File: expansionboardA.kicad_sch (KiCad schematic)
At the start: 40 parts, among them J1 USB-SERIAL, J3 HDMI_A, P1 USB_C_Plug, U1 MAX3420EECJ, U2 GPIO_U2, U3 AMS1117-3.3, U4 GPIO_U4, U5 MCP3008T-I/SL, U6 TLV320AIC23BIPW, Y1 Crystal

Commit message: Board updated
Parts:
- J1: value USB-SERIAL -> DEBUG
- renumbered MicroSDCard1 to CRD1
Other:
- note removed: "An expansion board for QMTECH A7200T core board"
- note removed: "QMTECH A7200T Board Expansion Module"
- note removed: "v0.1"
- moved on the sheet: ADC1, AU1, AU2, C1, C2, C3, C4, C5, C6, C7, D1, D2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

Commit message: Updated schematic with correct parts Built gerber files
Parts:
- C6, C7: footprint Capacitor_SMD:C_0603_1608Metric -> Capacitor_SMD:C_0805_2012Metric_Pad1.18x1.45mm_HandSolder
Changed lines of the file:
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@@
       (effects (font (size 1.27 1.27)) (justify left))
     )
-    (property "Footprint" "Capacitor_SMD:C_0603_1608Metric" (at 274.0152 49.53 0)
+    (property "Footprint" "Capacitor_SMD:C_0805_2012Metric_Pad1.18x1.45mm_HandSolder" (at 274.0152 49.53 0)
       (effects (font (size 1.27 1.27)) hide)
     )
@@
       (effects (font (size 1.27 1.27)) (justify left))
     )
-    (property "Footprint" "Capacitor_SMD:C_0603_1608Metric" (at 294.3352 49.53 0)
-      (effects (font (size 1.27 1.27)) hide)
-    )
+    (property "Footprint" "Capacitor_SMD:C_0805_2012Metric_Pad1.18x1.45mm_HandSolder" (at 294.3352 49.53 0)
+      (effects (font (size 1.27 1.27)) hide)
+    )

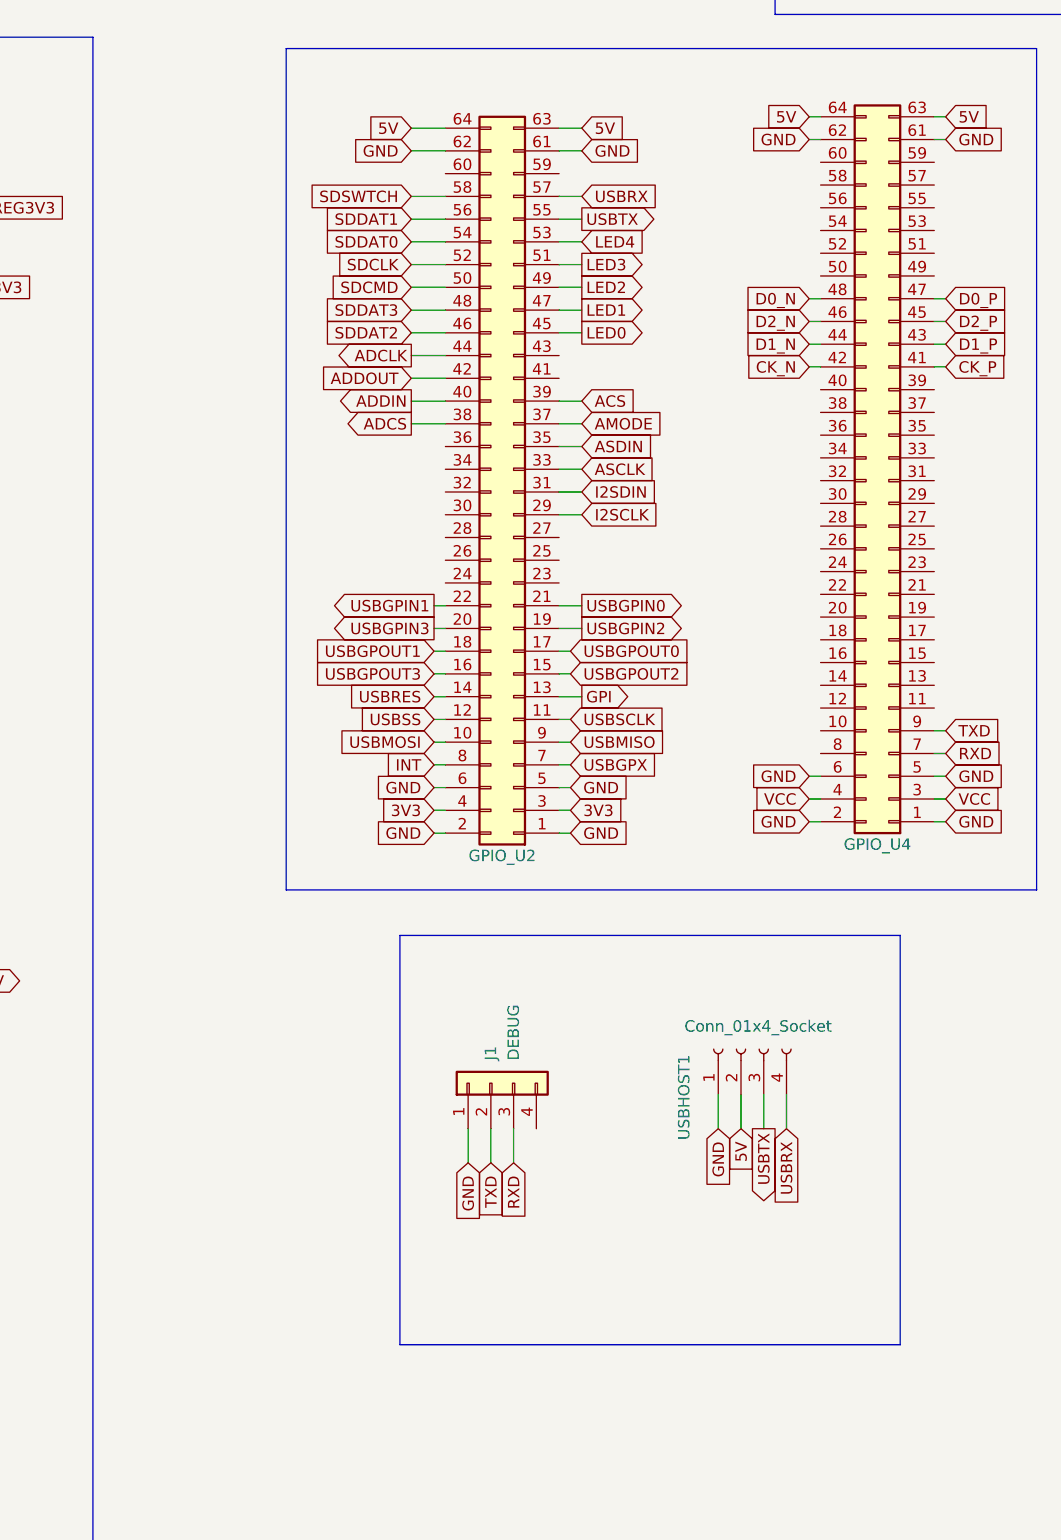
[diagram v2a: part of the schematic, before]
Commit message: Updated board with USB A host connector
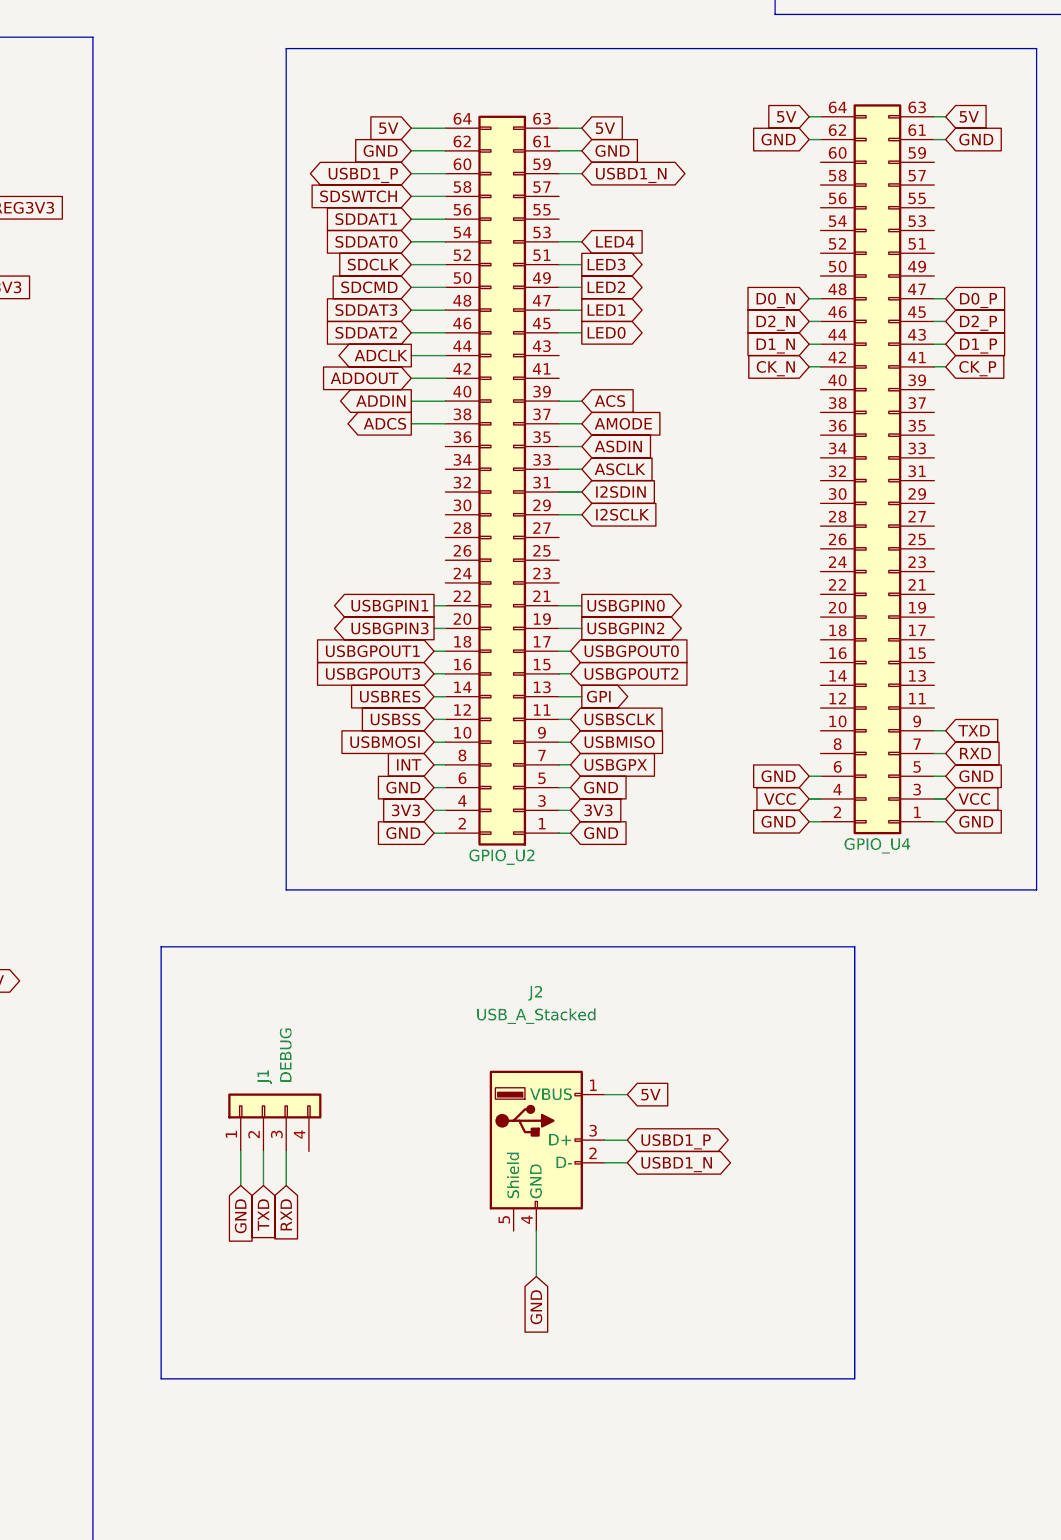
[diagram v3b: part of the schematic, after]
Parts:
- removed USBHOST1: Conn_01x4_Socket, Connector_PinSocket_2.54mm:PinSocket_1x04_P2.54mm_Horizontal, symbol Connector:Conn_01x04_Socket
- added J2: USB_A_Stacked, Connector_USB:USB_A_Molex_67643_Horizontal, symbol Connector:USB_A
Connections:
- net 5V: now also J2.1 (VBUS)
- net GND: now also J2.4 (GND)
- net USBD1_N: now reaches U2.59 (Pin_59)
- net USBD1_N: now also J2.2 (D-)
- net USBD1_P: now reaches U2.60 (Pin_60)
- net USBD1_P: now also J2.3 (D+)
- net USBRX: no longer names the net of U2.57 (Pin_57)
- net USBTX: no longer names the net of U2.55 (Pin_55)
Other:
- moved on the sheet: J1

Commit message: Updated board
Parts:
- C1, C2, C3, C4, C5: footprint Capacitor_SMD:C_0603_1608Metric -> Capacitor_SMD:C_0603_1608Metric_Pad1.08x0.95mm_HandSolder
- R1, R10, R2, R3, R4, R5, R6, R7, R9: footprint Resistor_SMD:R_0603_1608Metric -> Resistor_SMD:R_0603_1608Metric_Pad0.98x0.95mm_HandSolder
- U3: footprint Package_TO_SOT_SMD:SOT-89-3 -> Package_TO_SOT_SMD:SOT-89-3_Handsoldering

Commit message: Updatre board version
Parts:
- removed AU2: SJ-3523-SMT-TR, SJ-3523-SMT-TR:CUI_SJ-3523-SMT-TR, symbol SJ-3523-SMT-TR:SJ-3523-SMT-TR
- removed D6: LED, LED_SMD:LED_1206_3216Metric_Pad1.42x1.75mm_HandSolder, symbol Device:LED
- removed U6: TLV320AIC23BIPW, TLV320AIC23BIPW:SOP65P640X120-28N, symbol TLV320AIC23BIPW:TLV320AIC23BIPW
- added C10: 0.1uf, Capacitor_SMD:C_0603_1608Metric_Pad1.08x0.95mm_HandSolder, symbol Device:C
- added C11, C13, C14: 3.3uf, Capacitor_THT:CP_Radial_D5.0mm_P2.50mm, symbol Device:C_Polarized_US
- added C12: 10uf, Capacitor_THT:CP_Radial_D5.0mm_P2.50mm, symbol Device:C_Polarized_US
- added C8, C9: 1uf ceramic, Capacitor_SMD:C_0603_1608Metric_Pad1.08x0.95mm_HandSolder, symbol Device:C
- added R11, R14: 10KOhm, Resistor_SMD:R_0603_1608Metric_Pad0.98x0.95mm_HandSolder, symbol Device:R
- added R12, R13: 470Ohm, Resistor_SMD:R_0603_1608Metric_Pad0.98x0.95mm_HandSolder, symbol Device:R
- added R8: R33_ohm, Resistor_SMD:R_0603_1608Metric_Pad0.98x0.95mm_HandSolder, symbol Device:R
- added U6: CS4344-CZZR, CIR_3TSSOP-10, symbol 2023-04-16_23-08-01:CS4344-CZZR
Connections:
- net HPOUTLEFT is gone; now on an unnamed net: AU1.3
- net GND: now also C10.2, C11.2, C12.2, C8.1, C9.2, R11.2, R14.2, U6.8 (GND)
- net at R7.2: now also C8.2
- net ACS: no longer names the net of U2.39 (Pin_39)
- net AMODE: no longer names the net of U2.37 (Pin_37)
- net ASCLK renamed AU_LRCLK
- net AU_LRCLK: now also U6.3 (LRCK)
- net ASDIN renamed AU_MCLK
- net AU_MCLK: now also U6.4 (MCLK)
- net HPOUTRIGHT: no longer names the net of AU1.2
- net HPOUTRIGHT: now also C9.1, R8.2
- net I2SCLK renamed AU_SDIN
- net AU_SDIN: now also U6.1 (SDIN)
- net I2SDIN renamed AU_SCLK
- net AU_SCLK: now also U6.2 (*DEM/SCLK)
- net LED4: no longer names the net of U2.53 (Pin_53)
- net LED4: no longer R7.1
- new net: C13.2, R11.1, R12.1
- new net: C14.2, R13.1, R14.1
- new net: C12.1, U6.6 (FILT+)
- new net: C10.1, C11.1, U6.5 (VQ)
- new net AL: C14.1, U6.7 (AOUTL)
- new net AR: C13.1, U6.10 (AOUTR)
- new net LEFTOUT: R13.2, R7.1
- new net RIGHTOUT: R12.2, R8.1
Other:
- note added: "3v3 Power Regulator"
- note added: "Analog / Digital converter"
- note added: "Audio Out"
- note added: "Audio Output"
- note added: "DVI out over HDMI"
- note added: "Debug LEDs"
- note added: "FPGA board GPIO pins"
- note added: "Micro SD Card"
- note added: "Serial Debug Port"
- note added: "USB-A Host socket"
- note added: "USB-C Power and Data"
- moved on the sheet: ADC1, AU1, C1, C2, C3, C4, C5, C6, C7, CRD1, D1, D2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

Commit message: Updated board to fix some issues
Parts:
- added J4: FAN, Connector_PinHeader_2.54mm:PinHeader_1x02_P2.54mm_Vertical, symbol Connector_Generic:Conn_01x02
- J1: footprint Connector_PinSocket_2.54mm:PinSocket_1x04_P2.54mm_Vertical -> Connector_PinSocket_2.54mm:PinSocket_1x04_P2.54mm_Horizontal
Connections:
- net 5V: now also J4.2 (Pin_2)
- net GND: now also J4.1 (Pin_1)
- net input3v3: now also U6.9 (VA)
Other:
- note added: "FPGA Fan"
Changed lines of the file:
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@@
+    (stroke (width 0) (type default))
+  )
+  (wire (pts (xy 172.72 125.73) (xy 172.72 128.27))
     (stroke (width 0) (type default))
   )
@@
     (stroke (width 0) (type default))
   )
+  (wire (pts (xy 379.73 27.94) (xy 383.54 27.94))
+    (stroke (width 0) (type default))
+  )
   (wire (pts (xy 102.87 114.3) (xy 105.41 114.3))
     (stroke (width 0) (type default))
@@
     (stroke (width 0) (type default))
   )
+  (wire (pts (xy 170.18 125.73) (xy 170.18 128.27))
+    (stroke (width 0) (type default))
+  )
   (wire (pts (xy 226.06 53.34) (xy 241.3 53.34))
     (stroke (width 0) (type default))
@@
   )
   (rectangle (start 214.63 15.24) (end 280.67 60.96)
+    (stroke (width 0) (type default))
+    (fill (type none))
+  )
+  (rectangle (start 160.02 111.76) (end 182.88 137.16)
     (stroke (width 0) (type default))
     (fill (type none))
@@
     (effects (font (size 1.27 1.27)) (justify left bottom))
   )
+  (text "FPGA Fan" (at 161.29 114.3 0)
+    (effects (font (size 1.27 1.27)) (justify left bottom))
+  )
   (text "Analog / Digital converter" (at 82.55 17.78 0)
     (effects (font (size 1.27 1.27)) (justify left bottom))
@@
     (effects (font (size 1.27 1.27)) (justify left bottom))
   )
-  (label "input3v3" (at 377.19 27.94 0) (fields_autoplaced)
+  (label "input3v3" (at 383.54 27.94 0) (fields_autoplaced)
     (effects (font (size 1.27 1.27)) (justify left bottom))
   )
@@
     )
   )
+  (global_label "GND" (shape input) (at 170.18 128.27 270) (fields_autoplaced)
+    (effects (font (size 1.27 1.27)) (justify right))
+    (property "Intersheetrefs" "${INTERSHEET_REFS}" (at 170.18 135.0463 90)
+      (effects (font (size 1.27 1.27)) (justify right) hide)
+    )
+  )
   (global_label "GPI" (shape input) (at 308.61 101.6 180) (fields_autoplaced)
     (effects (font (size 1.27 1.27)) (justify right))
@@
     (property "Intersheetrefs" "${INTERSHEET_REFS}" (at 396.6663 45.72 0)
       (effects (font (size 1.27 1.27)) (justify left) hide)
+    )
+  )
+  (global_label "5V" (shape input) (at 172.72 128.27 270) (fields_autoplaced)
+    (effects (font (size 1.27 1.27)) (justify right))
+    (property "Intersheetrefs" "${INTERSHEET_REFS}" (at 172.72 133.4739 90)
+      (effects (font (size 1.27 1.27)) (justify right) hide)
     )
   )
@@
       (effects (font (size 1.27 1.27)) (justify left))
     )
-    (property "Footprint" "Connector_PinSocket_2.54mm:PinSocket_1x04_P2.54mm_Vertical" (at 171.45 82.55 0)
+    (property "Footprint" "Connector_PinSocket_2.54mm:PinSocket_1x04_P2.54mm_Horizontal" (at 171.45 82.55 0)
       (effects (font (size 1.27 1.27)) hide)
     )
@@
         )
       )
+    )
+  )
+  (symbol (lib_id "Connector_Generic:Conn_01x02") (at 170.18 120.65 90) (unit 1)
+    (in_bom yes) (on_board yes) (dnp no)
+    (property "Reference" "J4" (at 170.1799 118.11 0)
+      (effects (font (size 1.27 1.27)) (justify left))
+    )
+    (property "Value" "FAN" (at 172.7199 118.11 0)
+      (effects (font (size 1.27 1.27)) (justify left))
+    )
+    (property "Footprint" "Connector_PinHeader_2.54mm:PinHeader_1x02_P2.54mm_Vertical" (at 170.18 120.65 0)
+      (effects (font (size 1.27 1.27)) hide)
+    )
+    (property "Datasheet" "~" (at 170.18 120.65 0)
+      (effects (font (size 1.27 1.27)) hide)
+    )
+    (pin "1")
+    (pin "2")
+    (instances
+      (project "expansionboardA"
+        (path "/317f7f3e-4535-46d0-9a87-af1bea12706a"
+          (reference "J4") (unit 1)
+        )
+      )

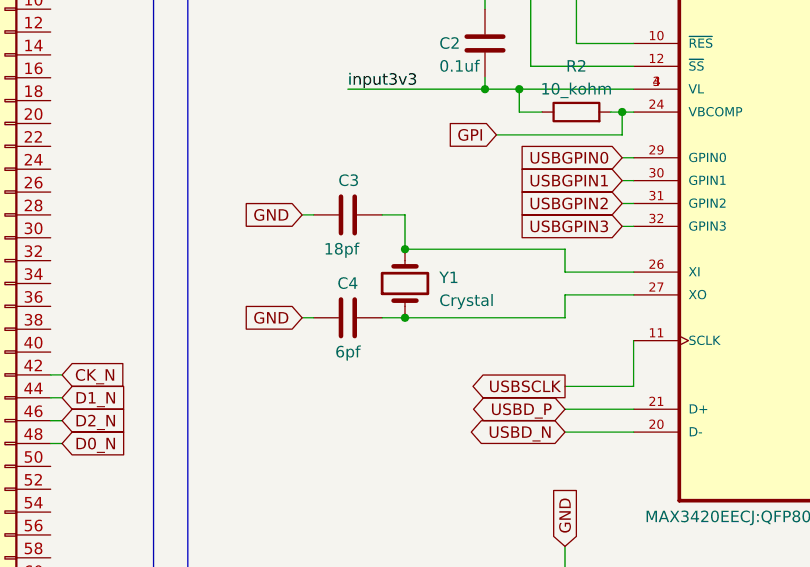
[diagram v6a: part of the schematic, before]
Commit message: Updated to new board version
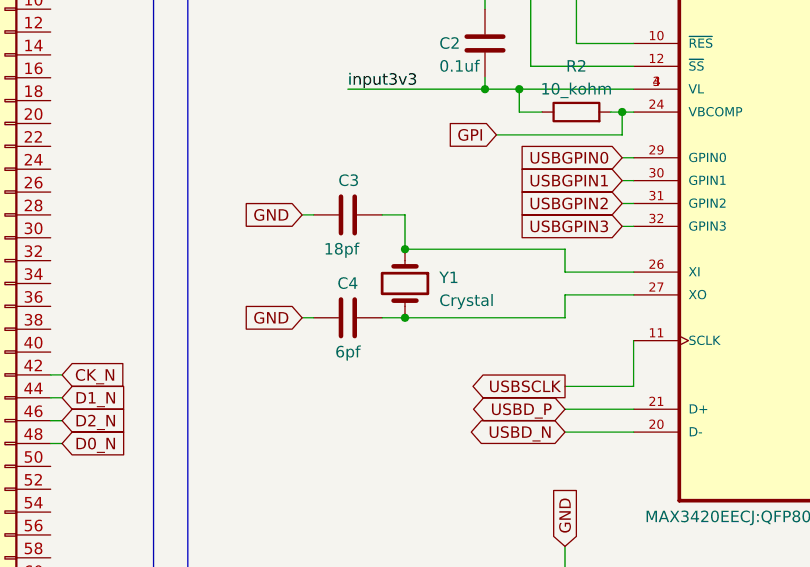
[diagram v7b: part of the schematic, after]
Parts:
- C11, C13, C14: footprint Capacitor_THT:CP_Radial_D5.0mm_P2.50mm -> Capacitor_THT:CP_Radial_D10.0mm_P5.00mm
- C12: footprint Capacitor_THT:CP_Radial_D5.0mm_P2.50mm -> Capacitor_SMD:CP_Elec_6.3x5.9
- R11, R14: footprint Resistor_SMD:R_0603_1608Metric_Pad0.98x0.95mm_HandSolder -> Resistor_THT:R_Axial_DIN0207_L6.3mm_D2.5mm_P7.62mm_Horizontal
- R12, R13: footprint Resistor_SMD:R_0603_1608Metric_Pad0.98x0.95mm_HandSolder -> Resistor_THT:R_Axial_DIN0204_L3.6mm_D1.6mm_P5.08mm_Horizontal
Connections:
- net at C4.2, U1.27 (XO): now also Y1.2; no longer Y1.1
- net at C3.2, U1.26 (XI): now also Y1.1; no longer Y1.2
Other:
- moved on the sheet: Y1
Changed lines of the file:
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@@
   (junction (at 100.33 57.15) (diameter 0) (color 0 0 0 0)
   )
+  (junction (at 298.45 121.92) (diameter 0) (color 0 0 0 0)
+  )
   (junction (at 359.41 57.15) (diameter 0) (color 0 0 0 0)
   )
@@
   (junction (at 323.85 57.15) (diameter 0) (color 0 0 0 0)
   )
-  (junction (at 298.45 121.92) (diameter 0) (color 0 0 0 0)
-  )
   (junction (at 264.16 27.94) (diameter 0) (color 0 0 0 0)
   )
-  (junction (at 119.38 119.38) (diameter 0) (color 0 0 0 0)
-  )
   (junction (at 298.45 114.3) (diameter 0) (color 0 0 0 0)
   )
+  (junction (at 119.38 119.38) (diameter 0) (color 0 0 0 0)
+  )
   (junction (at 307.34 96.52) (diameter 0) (color 0 0 0 0)
   )
@@
     (stroke (width 0) (type default))
   )
-  (wire (pts (xy 298.45 121.92) (xy 316.23 121.92))
+  (wire (pts (xy 295.91 121.92) (xy 298.45 121.92))
     (stroke (width 0) (type default))
   )
@@
     (stroke (width 0) (type default))
   )
-  (wire (pts (xy 295.91 121.92) (xy 298.45 121.92))
-    (stroke (width 0) (type default))
-  )
   (wire (pts (xy 264.16 53.34) (xy 264.16 50.8))
     (stroke (width 0) (type default))
@@
     (stroke (width 0) (type default))
   )
+  (wire (pts (xy 298.45 121.92) (xy 316.23 121.92))
+    (stroke (width 0) (type default))
+  )
   (wire (pts (xy 177.8 40.64) (xy 182.88 40.64))
     (stroke (width 0) (type default))
@@
     )
   )
-  (symbol (lib_id "Device:Crystal") (at 298.45 118.11 90) (unit 1)
+  (symbol (lib_id "Device:Crystal") (at 298.45 118.11 270) (unit 1)
     (in_bom yes) (on_board yes) (dnp no) (fields_autoplaced)
     (property "Reference" "Y1" (at 302.26 117.475 90)
-      (effects (font (size 1.27 1.27)) (justify right))
+      (effects (font (size 1.27 1.27)) (justify left))
     )
     (property "Value" "Crystal" (at 302.26 120.015 90)
-      (effects (font (size 1.27 1.27)) (justify right))
+      (effects (font (size 1.27 1.27)) (justify left))
     )
     (property "Footprint" "Crystal:Crystal_AT310_D3.0mm_L10.0mm_Horizontal" (at 298.45 118.11 0)
@@
       (effects (font (size 1.27 1.27)))
     )
-    (property "Footprint" "Resistor_SMD:R_0603_1608Metric_Pad0.98x0.95mm_HandSolder" (at 328.93 58.928 90)
+    (property "Footprint" "Resistor_THT:R_Axial_DIN0207_L6.3mm_D2.5mm_P7.62mm_Horizontal" (at 328.93 58.928 90)
       (effects (font (size 1.27 1.27)) hide)
     )
@@
       (effects (font (size 1.27 1.27)))
     )
-    (property "Footprint" "Resistor_SMD:R_0603_1608Metric_Pad0.98x0.95mm_HandSolder" (at 364.49 51.308 90)
+    (property "Footprint" "Resistor_THT:R_Axial_DIN0204_L3.6mm_D1.6mm_P5.08mm_Horizontal" (at 364.49 51.308 90)
       (effects (font (size 1.27 1.27)) hide)
     )
@@
       (effects (font (size 1.27 1.27)))
     )
-    (property "Footprint" "Capacitor_THT:CP_Radial_D5.0mm_P2.50mm" (at 387.35 39.37 0)
+    (property "Footprint" "Capacitor_SMD:CP_Elec_6.3x5.9" (at 387.35 39.37 0)
       (effects (font (size 1.27 1.27)) hide)
     )
@@
       (effects (font (size 1.27 1.27)))
     )
-    (property "Footprint" "Resistor_SMD:R_0603_1608Metric_Pad0.98x0.95mm_HandSolder" (at 364.49 58.928 90)
+    (property "Footprint" "Resistor_THT:R_Axial_DIN0207_L6.3mm_D2.5mm_P7.62mm_Horizontal" (at 364.49 58.928 90)
       (effects (font (size 1.27 1.27)) hide)
     )
@@
       (effects (font (size 1.27 1.27)))
     )
-    (property "Footprint" "Capacitor_THT:CP_Radial_D5.0mm_P2.50mm" (at 318.77 57.15 0)
+    (property "Footprint" "Capacitor_THT:CP_Radial_D10.0mm_P5.00mm" (at 318.77 57.15 0)
       (effects (font (size 1.27 1.27)) hide)
     )
@@
       (effects (font (size 1.27 1.27)))
     )
-    (property "Footprint" "Capacitor_THT:CP_Radial_D5.0mm_P2.50mm" (at 354.33 57.15 0)
+    (property "Footprint" "Capacitor_THT:CP_Radial_D10.0mm_P5.00mm" (at 354.33 57.15 0)
       (effects (font (size 1.27 1.27)) hide)
     )
@@
       (effects (font (size 1.27 1.27)))
     )
-    (property "Footprint" "Resistor_SMD:R_0603_1608Metric_Pad0.98x0.95mm_HandSolder" (at 328.93 51.308 90)
+    (property "Footprint" "Resistor_THT:R_Axial_DIN0204_L3.6mm_D1.6mm_P5.08mm_Horizontal" (at 328.93 51.308 90)
       (effects (font (size 1.27 1.27)) hide)
     )
@@
       (effects (font (size 1.27 1.27)))
     )
-    (property "Footprint" "Capacitor_THT:CP_Radial_D5.0mm_P2.50mm" (at 309.88 41.91 0)
+    (property "Footprint" "Capacitor_THT:CP_Radial_D10.0mm_P5.00mm" (at 309.88 41.91 0)
       (effects (font (size 1.27 1.27)) hide)
     )
